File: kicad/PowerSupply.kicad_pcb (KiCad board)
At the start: 2 copper layers, 90 x 140 mm, 116 parts, among them J1 USB_A, J2 Display, Q1 MMBT3904, Q10 MMBT3904, Q11 MMBT3904, Q2 MMBT3904, Q3 MMBT3904, Q4 MMBT3904, Q5 MMBT3904, Q6 MMBT3904, Q7 MMBT3904, Q8 MMBT3904, Q9 MMBT3904, SW1 ENC0 (Voltage), SW2 ENC1 (Current), SW3 SW_DIP_x04, U1 OPA4196, U10 STM32F373C8Tx, U2 OPA4196, U3 LD1086D2T33, U4 LD1086D2T33, U5 FQP17P10, U6 FQP17P10, U7 FQP17P10, U8 FQP17P10

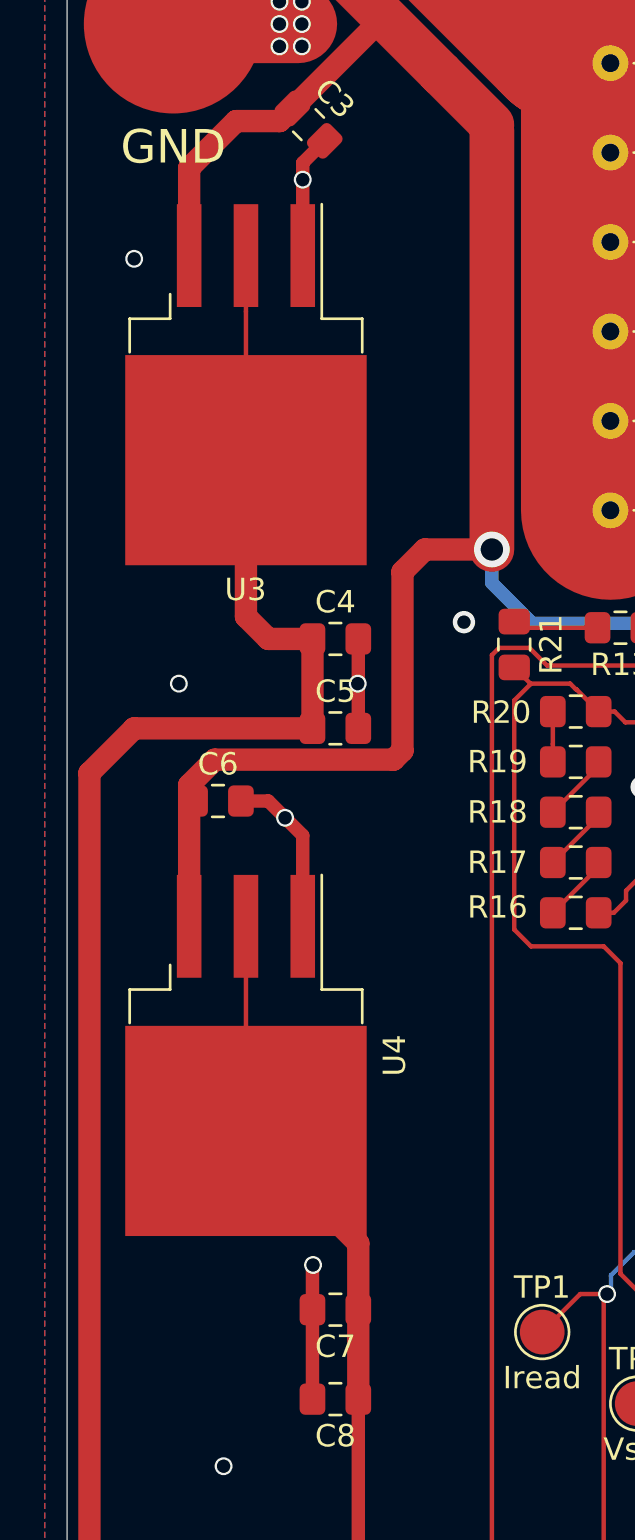
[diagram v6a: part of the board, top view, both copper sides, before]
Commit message: JK removed reduntant traces
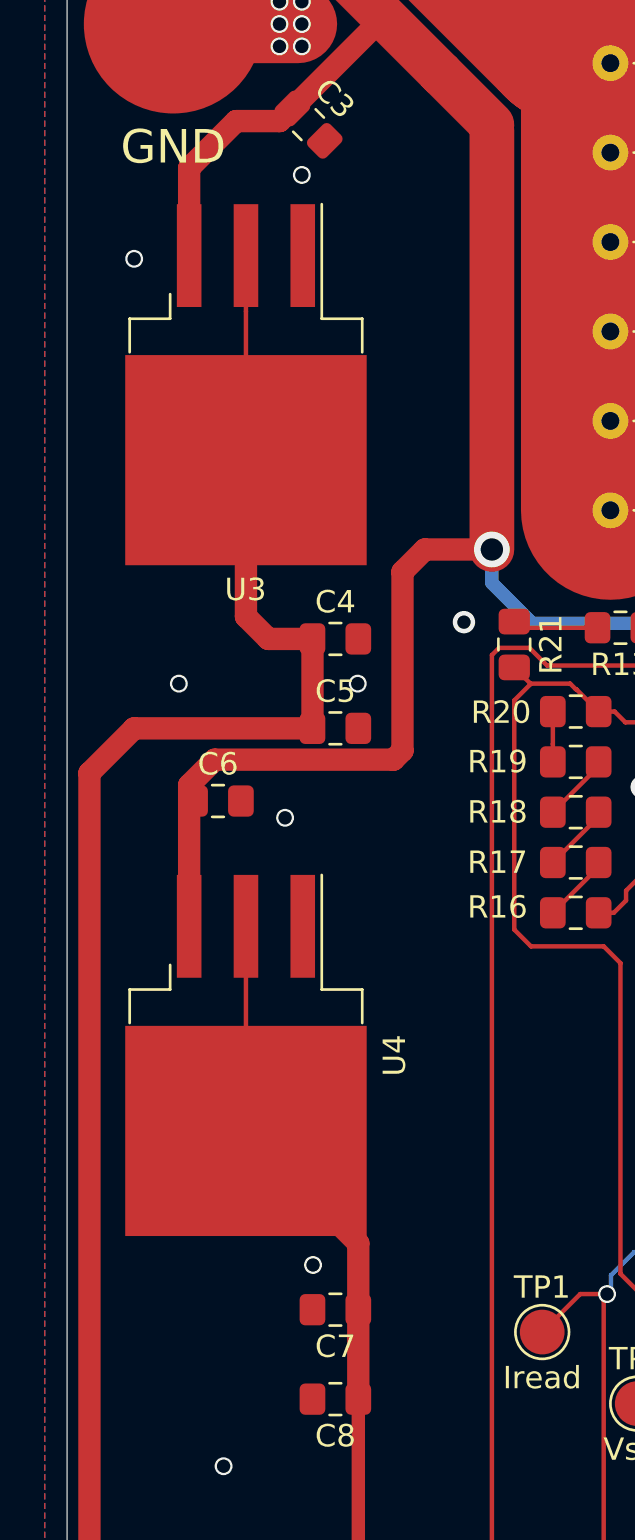
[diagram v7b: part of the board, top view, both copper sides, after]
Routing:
- net GNDREF: track 68.3 -> 45.3 mm
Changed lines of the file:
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@@
     (thickness 1.6)
     (drawings 11)
-    (tracks 1104)
+    (tracks 1094)
     (zones 0)
     (modules 116)
@@
   (via (at 38 79) (size 1) (drill 0.6) (layers F.Cu B.Cu) (net 1))
   (via (at 35.25 71.25) (size 1) (drill 0.6) (layers F.Cu B.Cu) (net 1))
-  (segment (start 10.54 32.709568) (end 11.524784 31.724784) (width 0.6) (layer F.Cu) (net 1))
-  (segment (start 10.54 36.855) (end 10.54 33.46) (width 0.6) (layer F.Cu) (net 1))
-  (segment (start 7.775 61.25) (end 9 61.25) (width 0.6) (layer F.Cu) (net 1))
-  (segment (start 9 61.25) (end 9.75 62) (width 0.6) (layer F.Cu) (net 1))
-  (segment (start 10.54 62.79) (end 10.54 66.855) (width 0.6) (layer F.Cu) (net 1))
-  (segment (start 9.75 62) (end 10.54 62.79) (width 0.6) (layer F.Cu) (net 1))
   (via (at 9.75 62) (size 0.8) (drill 0.6) (layers F.Cu B.Cu) (net 1))
-  (segment (start 10.54 33.46) (end 10.54 32.709568) (width 0.6) (layer F.Cu) (net 1))
-  (via (at 10.54 33.46) (size 0.8) (drill 0.6) (layers F.Cu B.Cu) (net 1))
-  (segment (start 13.025 58) (end 13.025 54) (width 0.6) (layer F.Cu) (net 1))
-  (segment (start 10.975 88) (end 10.975 84) (width 0.6) (layer F.Cu) (net 1))
   (via (at 11 82) (size 0.8) (drill 0.6) (layers F.Cu B.Cu) (net 1))
-  (segment (start 10.975 84) (end 10.975 82.025) (width 0.6) (layer F.Cu) (net 1))
   (segment (start 10.975 82.025) (end 11 82) (width 0.6) (layer F.Cu) (net 1))
   (segment (start 22 117.2) (end 22 119.5875) (width 0.2) (layer F.Cu) (net 1))
@@
   (via (at 66 31) (size 0.8) (drill 0.6) (layers F.Cu B.Cu) (net 1))
   (via (at 25.7 60.625) (size 1) (drill 0.6) (layers F.Cu B.Cu) (net 1))
+  (via (at 10.5 33.25) (size 0.8) (drill 0.6) (layers F.Cu B.Cu) (net 1))
   (segment (start 19.91863 15.5) (end 4.75 15.5) (width 8) (layer F.Cu) (net 2))
   (segment (start 4.75 15.5) (end 11 15.5) (width 8) (layer F.Cu) (net 2))

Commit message: Deleted the whole PCB to start over
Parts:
- removed C1, C12, C14, C17, C2, C20, C23, C24, C25, C5, C8: 100nF, Capacitor_SMD:C_0805_2012Metric_Pad1.15x1.40mm_HandSolder
- removed C10, C11, C3, C6: 10µF HV, Capacitor_SMD:C_0805_2012Metric_Pad1.15x1.40mm_HandSolder
- removed C13, C16, C19, C26: 10nF, Capacitor_SMD:C_0805_2012Metric_Pad1.15x1.40mm_HandSolder
- removed C15, C18, C21, C9: 1µF, Capacitor_SMD:C_0805_2012Metric_Pad1.15x1.40mm_HandSolder
- removed C22: 4.7µF, Capacitor_SMD:C_0805_2012Metric_Pad1.15x1.40mm_HandSolder
- removed C4, C7: 10µF, Capacitor_SMD:C_0805_2012Metric_Pad1.15x1.40mm_HandSolder
- removed D1: APTD3216LZGCK, LED_SMD:LED_1206_3216Metric_Pad1.42x1.75mm_HandSolder
- removed D2, D3, D4, D5, D6, D7, D8, D9: APTD3216LVBC/D, LED_SMD:LED_1206_3216Metric_Pad1.42x1.75mm_HandSolder
- removed HS1, HS2, HS3, HS4: RA-T2X-xxE, footprints:RA-T2X-xxE
- removed J1: USB_A, footprints:USBA
- removed J2: Display, Connector_PinHeader_2.54mm:PinHeader_1x16_P2.54mm_Vertical
- removed Q1, Q10, Q11, Q2, Q3, Q4, Q5, Q6, Q7, Q8, Q9: MMBT3904, Package_TO_SOT_SMD:SOT-23
- removed R1, R10, R2, R3, R4, R5, R6, R7, R8, R9: 1R, Resistor_THT:R_Axial_DIN0309_L9.0mm_D3.2mm_P12.70mm_Horizontal
- removed R11, R12, R16, R17, R18, R19, R20, R25, R26, R34: 10k, Resistor_SMD:R_0805_2012Metric_Pad1.15x1.40mm_HandSolder
- removed R13, R14: 82k5, Resistor_SMD:R_0805_2012Metric_Pad1.15x1.40mm_HandSolder
- removed R15, R27, R28, R29, R30, R31, R32, R33, R35, R36, R37, R38, R39, R40, R41, R42, R43: 1k, Resistor_SMD:R_0805_2012Metric_Pad1.15x1.40mm_HandSolder
- removed R21: 9k88, Resistor_SMD:R_0805_2012Metric_Pad1.15x1.40mm_HandSolder
- removed R22, R23, R24: ?, Resistor_SMD:R_0805_2012Metric_Pad1.15x1.40mm_HandSolder
- removed REF**: OSHW-Symbol_6.7x6mm_SilkScreen, Symbol:OSHW-Symbol_6.7x6mm_SilkScreen
- removed REF** (x3): SolderWirePad_1x01_Drill2mm, Connector_Wire:SolderWirePad_1x01_Drill2mm
- removed SW1: ENC0 (Voltage), footprints:PEC12R-2xxxf-Sxxxx
- removed SW2: ENC1 (Current), footprints:PEC12R-2xxxf-Sxxxx
- removed SW3: SW_DIP_x04, Button_Switch_THT:SW_DIP_SPSTx04_Piano_10.8x11.72mm_W7.62mm_P2.54mm
- removed TP1: Iread, TestPoint:TestPoint_Pad_D2.0mm
- removed TP2: Vread, TestPoint:TestPoint_Pad_D2.0mm
- removed TP3: Vreg, TestPoint:TestPoint_Pad_D2.0mm
- removed TP4: Vset, TestPoint:TestPoint_Pad_D2.0mm
- removed TP5: Iset, TestPoint:TestPoint_Pad_D2.0mm
- removed U1, U2: OPA4196, Package_SO:SOIC-14_3.9x8.7mm_P1.27mm
- removed U10: STM32F373C8Tx, Package_QFP:LQFP-48_7x7mm_P0.5mm
- removed U3, U4: LD1086D2T33, Package_TO_SOT_SMD:TO-263-3_TabPin2
- removed U5, U6, U7, U8: FQP17P10, Package_TO_SOT_THT:TO-220-3_Vertical
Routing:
- net /PassElement/Vout: track 339.5 -> 0.00 mm, vias 11 -> 0
- net +3V3: track 334.0 -> 0.00 mm, vias 8 -> 0
- net /PassElement/Vin: track 282.5 -> 0.00 mm
- net VDD: track 239.7 -> 0.00 mm, vias 7 -> 0
- net /Logic/CODE_B3: track 120.9 -> 0.00 mm, vias 4 -> 0
- net /PassElement/VReg_set: track 112.9 -> 0.00 mm
- net +3V3A: track 95.9 -> 0.00 mm, vias 3 -> 0
- net /Logic/CODE_B4: track 86.0 -> 0.00 mm, vias 4 -> 0
- net /Logic/Vread: track 82.0 -> 0.00 mm, vias 2 -> 0
- net /Logic/ENC0_B: track 81.1 -> 0.00 mm
- net /CurrentSense/Iread: track 76.0 -> 0.00 mm, vias 4 -> 0
- net /Logic/ENC0_A: track 74.8 -> 0.00 mm
- net /Logic/CODE_B0: track 68.2 -> 0.00 mm, vias 4 -> 0
- net Net-(J2-Pad10): track 67.5 -> 0.00 mm
- net Net-(J2-Pad12): track 67.2 -> 0.00 mm
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- removed copper zone on B.Cu, net GNDREF
- removed copper zone on F.Cu, net GNDREF
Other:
- board outline removed
- board text removed: "Current"
- board text removed: "GND"
- board text removed: "Output"
- board text removed: "REV 1"
- board text removed: "VCC"
- board text removed: "Voltage"
- board text removed: "Vout"
